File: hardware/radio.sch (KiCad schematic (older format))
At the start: 19 parts, among them U3 AT86RF231, Y1 NX3225SA-16MHz-15ppm

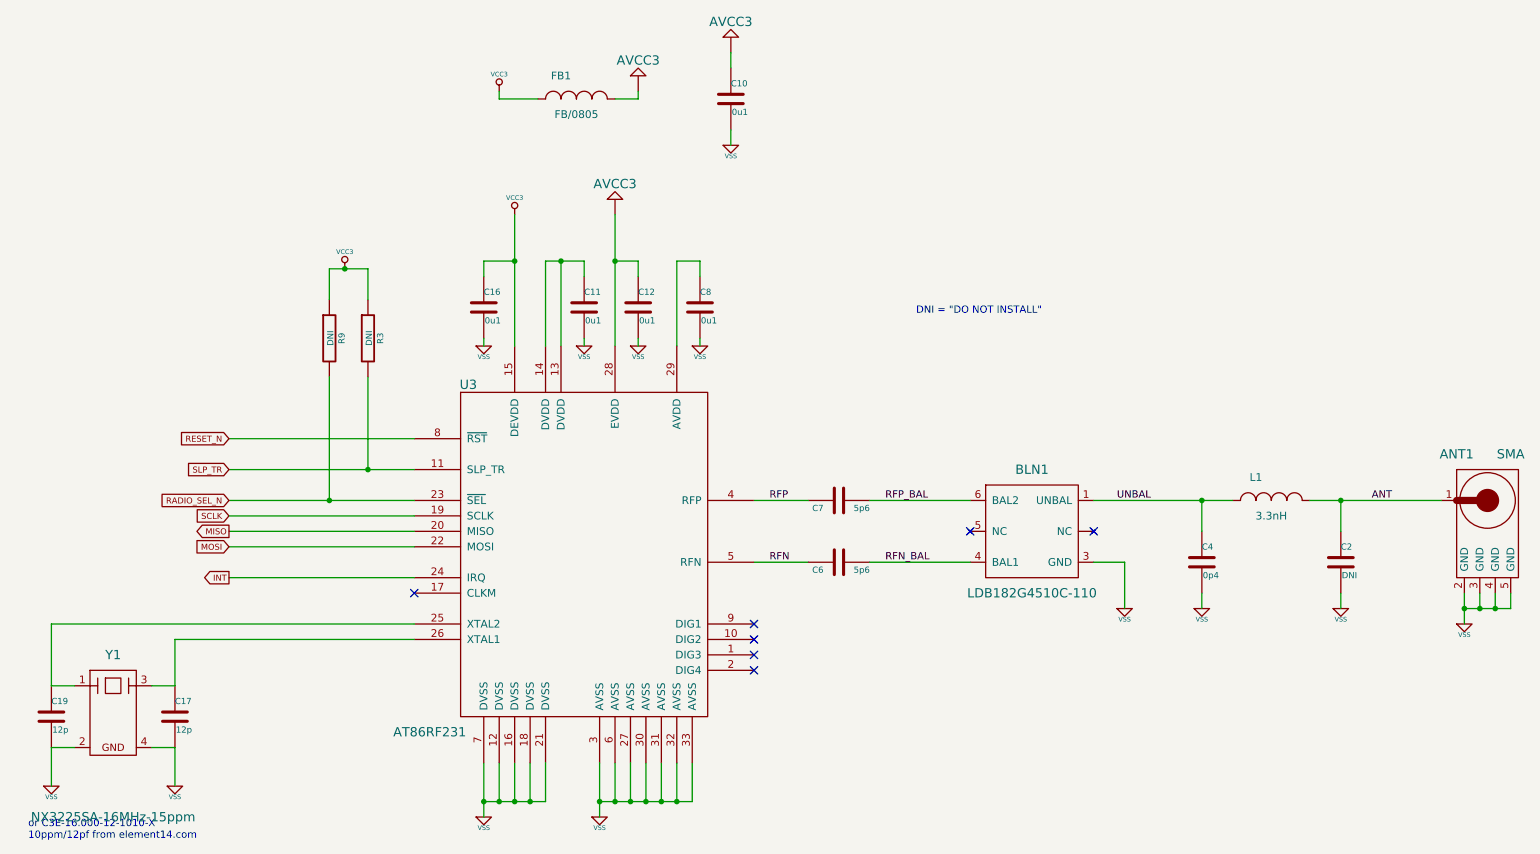
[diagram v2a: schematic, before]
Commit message: Balun chosen -- different to original Freakduino -- as 0805 part from Johanson Technology (Ex. element14). The pin connection layout is also different.
PCB footprint and 3D package for balun added.

Balun data sheet added.
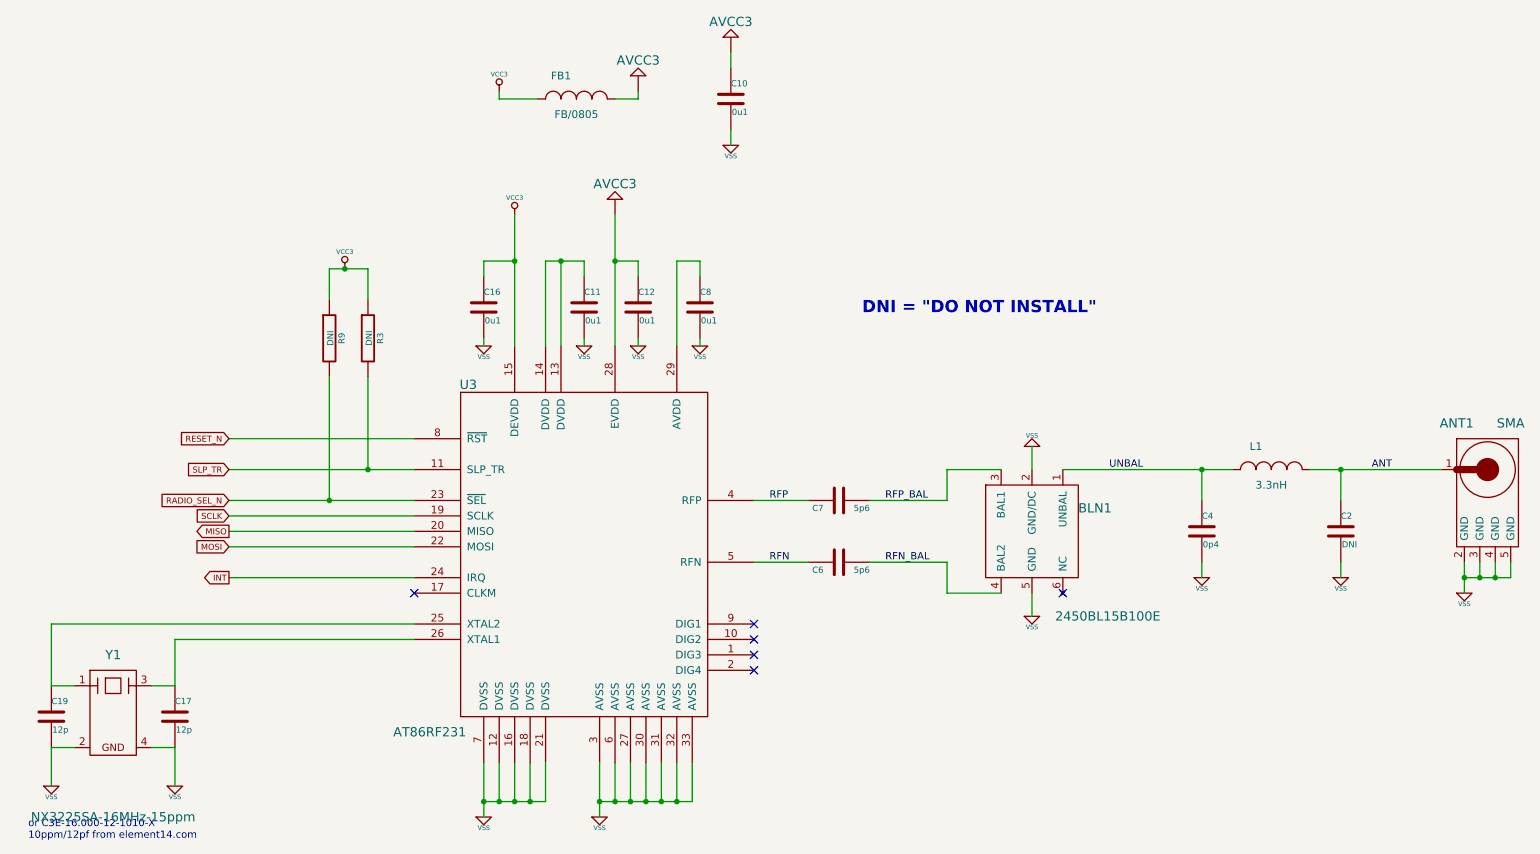
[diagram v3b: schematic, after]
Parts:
- removed BLN1: LDB182G4510C-110, symbol LDB182G4510C-110
- added BLN1: 2450BL15B100E, ~, symbol BALUN_GRUVIN
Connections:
- net RFN_BAL: now also BLN1.4 (BAL2)
- net RFP_BAL: now also BLN1.3 (BAL1)
- net UNBAL: now also BLN1.1 (UNBAL)
- net VSS: now also BLN1.2 (GND/DC), BLN1.5 (GND)
- no-connect marks 7 -> 6
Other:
- moved on the sheet: ANT1, C2, C4, L1
